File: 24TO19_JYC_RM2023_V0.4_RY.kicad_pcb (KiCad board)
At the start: 2 copper layers, 35 x 63 mm, 41 parts, among them J1 Conn_01x02, Q1 BSC070N10NS5, Q2 BSC070N10NS5, U1 LM3150MH

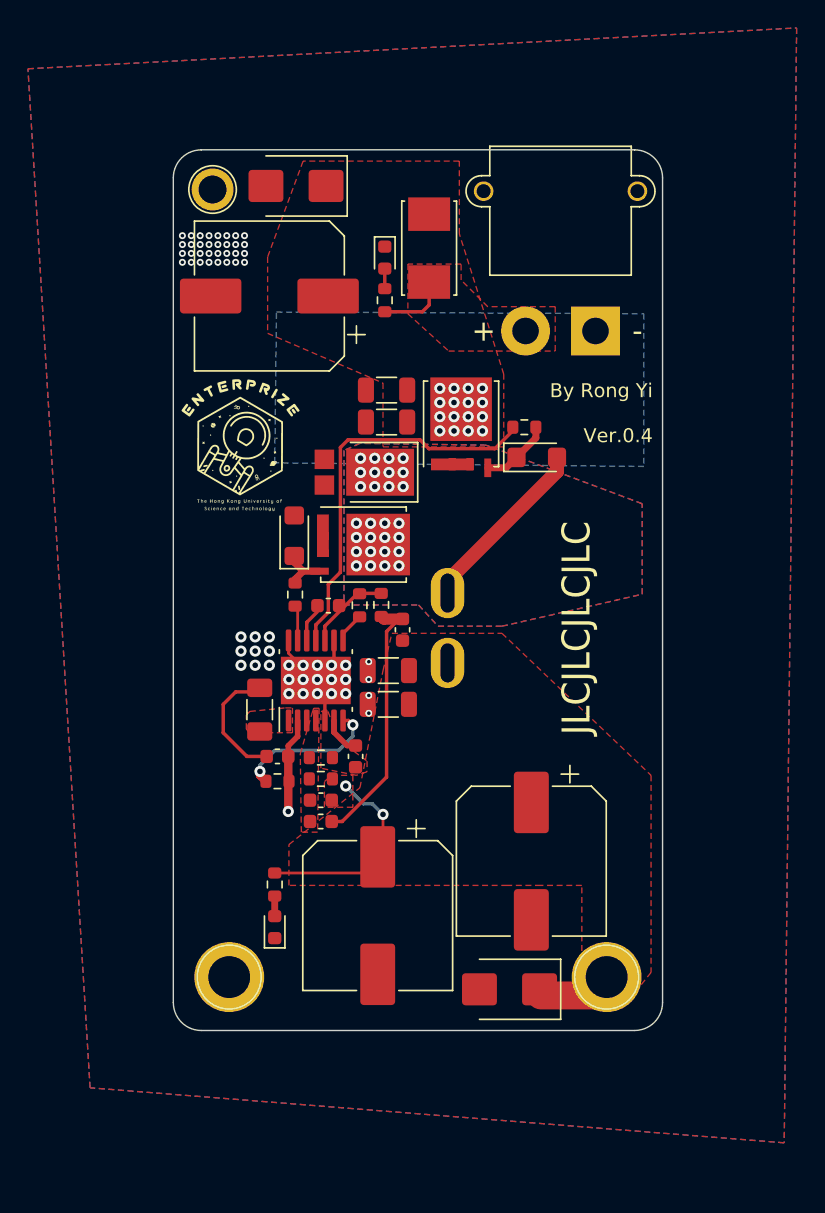
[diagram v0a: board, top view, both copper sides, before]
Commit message: decoration location adjustment build
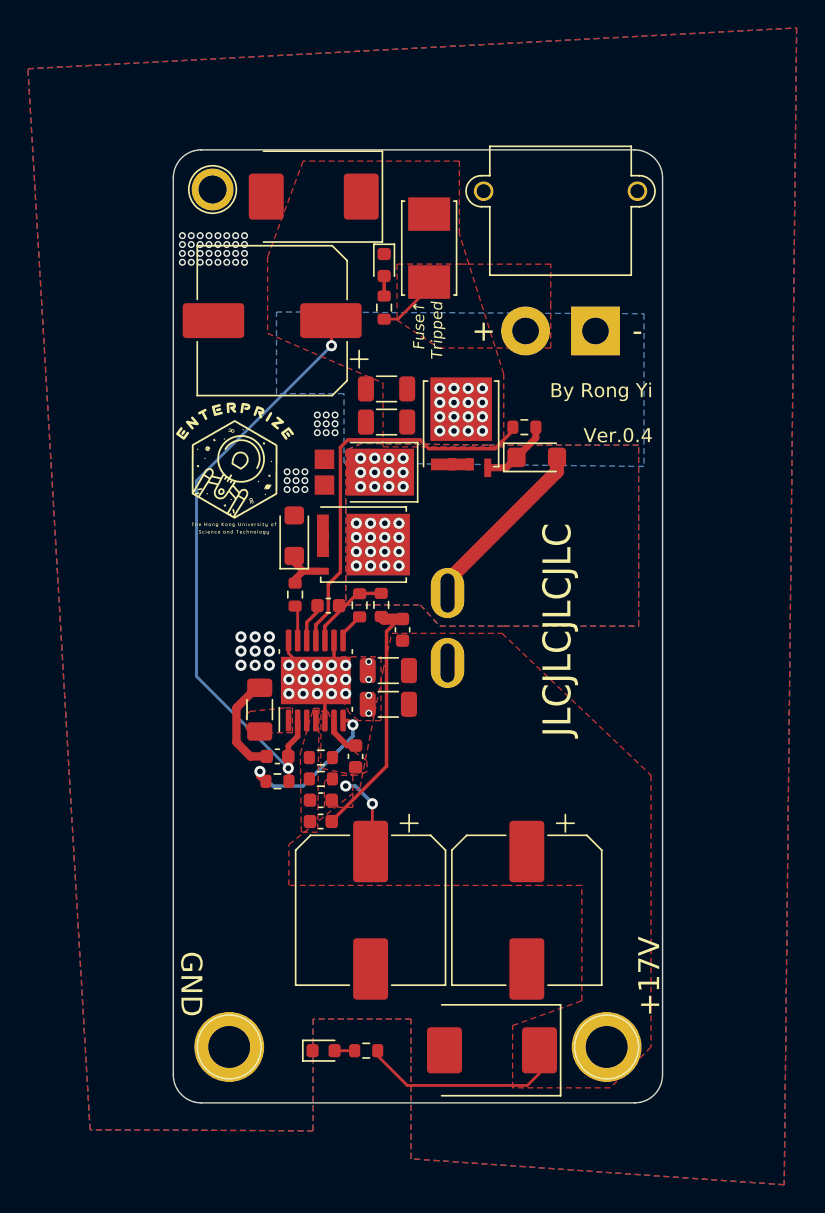
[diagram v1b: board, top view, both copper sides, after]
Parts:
- D1, D2: footprint Diode_SMD:D_SMB -> Diode_SMD:D_SMC
- moved R9 13.6 mm to (135.6, 119.3), turned to 180 degrees
- moved D3 9.50 mm to (132.5, 119.3), turned to 0 degrees
- moved TP1 5.00 mm to (125.8, 119.0)
- moved TP2 5.00 mm to (152.8, 119.0)
- moved D1 4.54 mm to (144.6, 119.2)
- moved C4 3.53 mm to (147.1, 109.2)
- moved G*** 1.78 mm to (129.1, 84.0)
- moved C6 1.77 mm to (128.9, 67.0)
- moved G*** 1.72 mm to (126.0, 77.5)
- moved D2 1.48 mm to (131.8, 58.2)
- moved C11 0.64 mm to (135.9, 109.2)
- moved R6 0.53 mm to (136.9, 66.1)
- moved D7 0.53 mm to (136.9, 63.1)
- moved C12 0.08 mm to (137.0, 71.9)
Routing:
- net +24V: track 6.79 -> 43.4 mm, vias 17 -> 18
- net /VOUT: track 20.5 -> 22.6 mm
- net GND: track 16.4 -> 14.7 mm, vias 60 -> 78
- net Net-(U1-RON): track 10.5 -> 11.1 mm
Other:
- board size 35 x 63 mm -> 35 x 68.2 mm
- board text added: "+17V"
- board text added: "24V→17V DCDC Module MiniPC Power Supply 10A MAX RM2023"
- board text added: "Fuse↑ Tripped"
- board text added: "GND"
